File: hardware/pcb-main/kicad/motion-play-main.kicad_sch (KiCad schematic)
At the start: 26 parts, among them J2 DWEII Power Module, J3 LED_Strip, J4 Conn_01x05, J5 Conn_01x05, J6 Conn_01x05, U1 AP2112K-3.3TRG1, U2 T-Display-S3

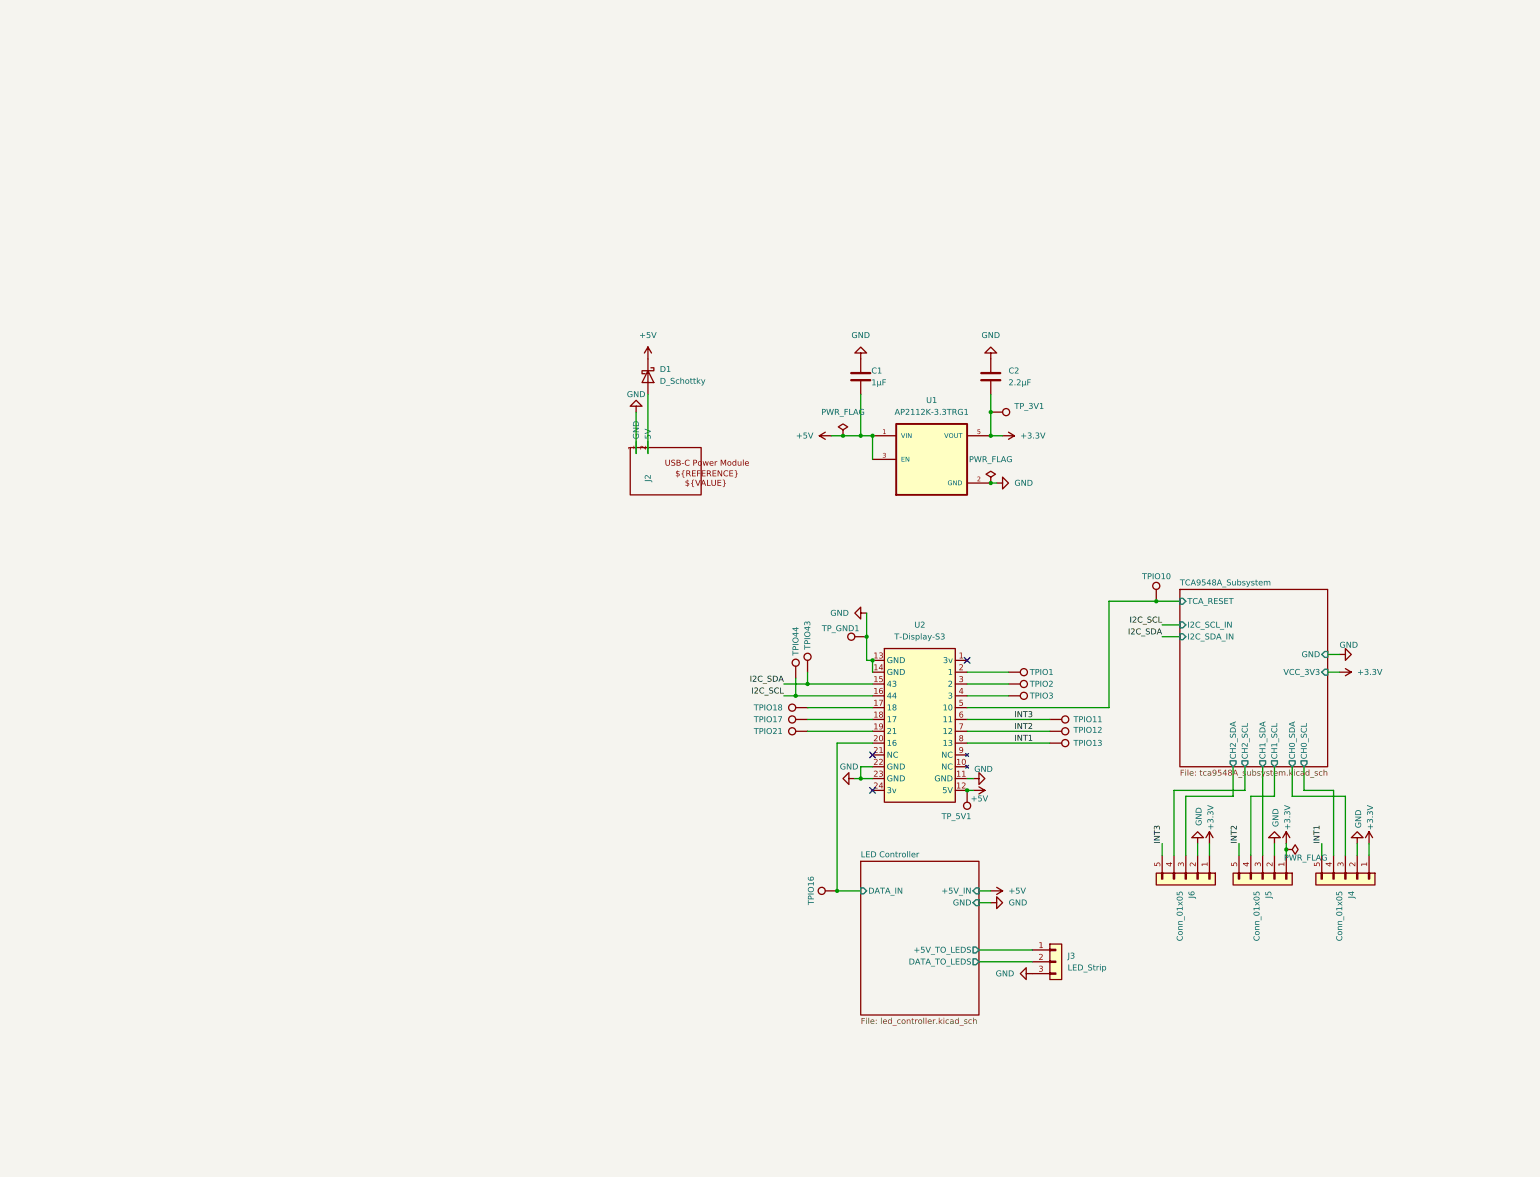
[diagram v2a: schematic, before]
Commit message: Complete Phase 3a: annotate power, MCU, I2C mux, and sensor connector blocks
Annotated 31/37 components across 4 functional blocks (power, mcu, i2c_mux,
sensor_connectors) with ai_function, ai_block, ai_role, and ai_critical_specs
properties. Remaining 6 components are LED controller block (Phase 3b).
Added 10 verification test questions for Phase 3c. KiCad round-trip confirmed
all ai_ properties survive native save.

Made-with: Cursor
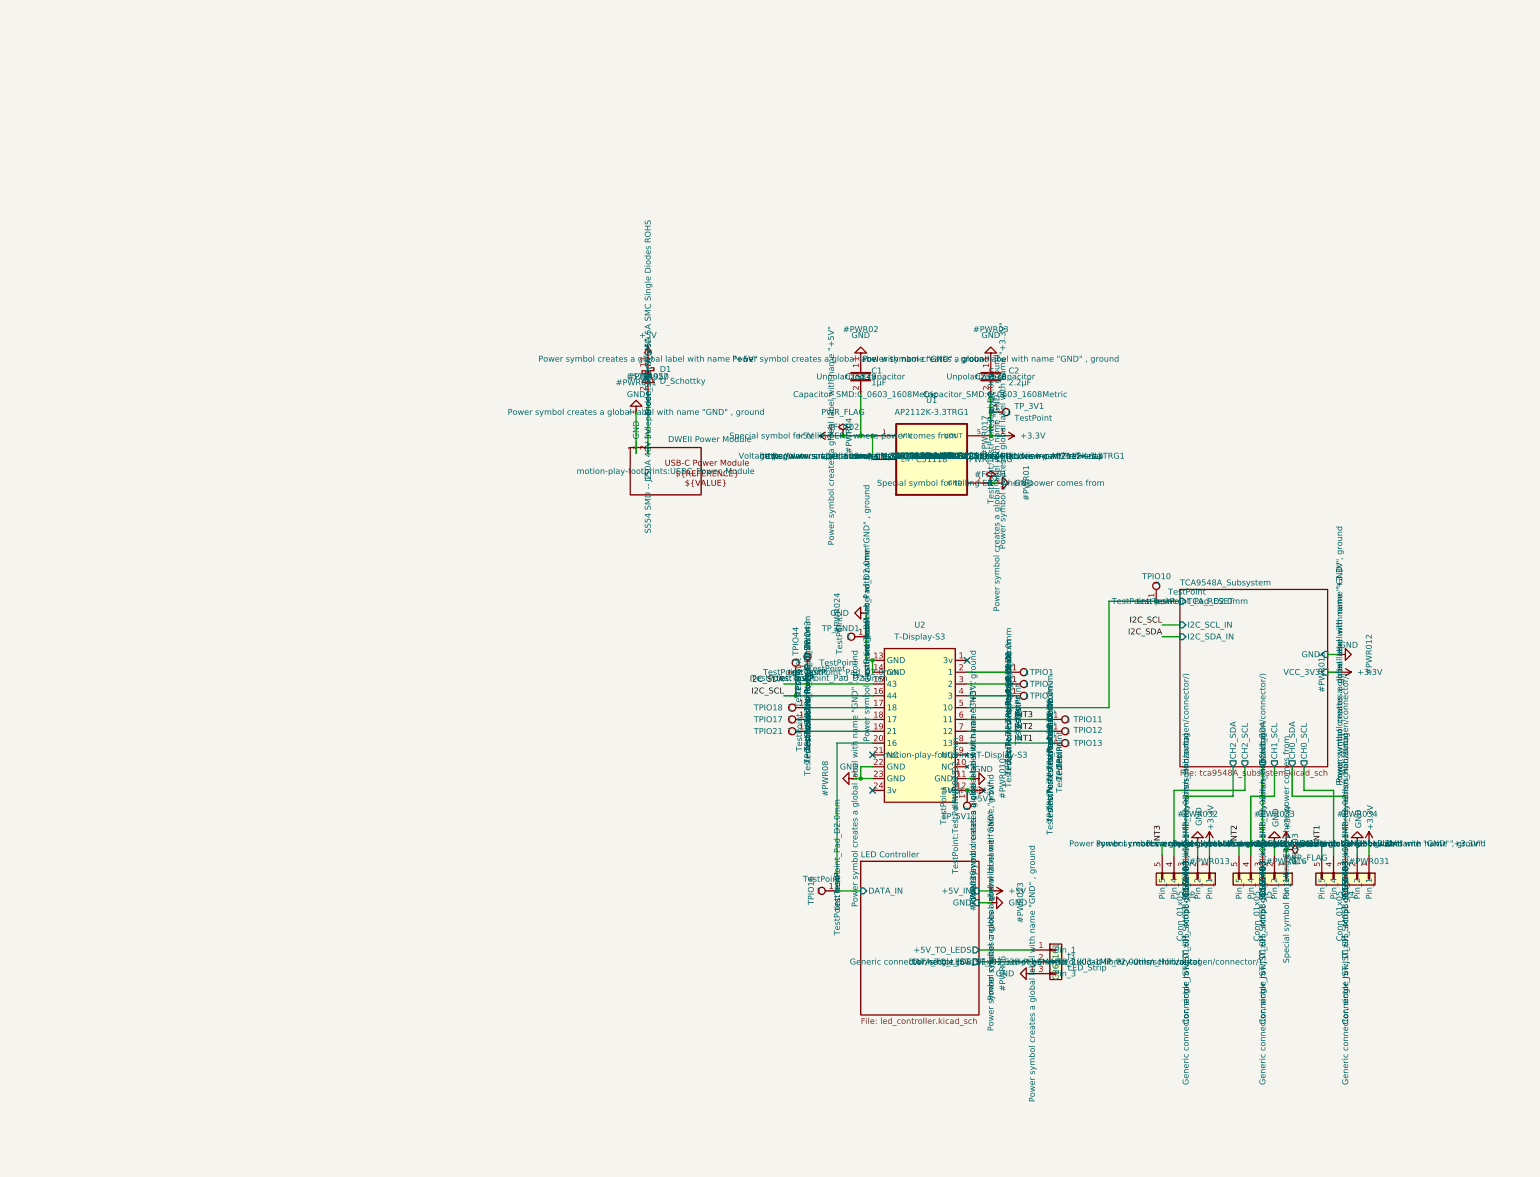
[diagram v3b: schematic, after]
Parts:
- C1: ai_block (none) -> power; ai_critical_specs (none) -> 1uF, 0603; ai_function (none) -> Input bypass capacitor for U1 voltage regulator; ai_role (none) -> decoupling
- C2: ai_block (none) -> power; ai_critical_specs (none) -> 2.2uF, 0603, required for LDO stability; ai_function (none) -> Output stabilization capacitor for U1 voltage regulator; ai_role (none) -> decoupling
- D1: ai_block (none) -> power; ai_critical_specs (none) -> Schottky, low Vf (~0.3V), handles full system current; ai_function (none) -> Reverse-polarity protection diode between power module and 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; ai_role (none) -> protection
- J2: ai_block (none) -> power; ai_critical_specs (none) -> 5V output, ~2.4A max, includes battery charging circuit; ai_function (none) -> USB-C power input module with battery charging, provides 5V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
- J4: ai_block (none) -> sensor_connectors; ai_critical_specs (none) -> 5-pin: 3.3V, GND, CH0_SDA, CH0_SCL, INT1; ai_function (none) -> JST-SH connector to sensor module 1 (M1, 6 oclock position)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; ai_role (none) -> connector
- J5: ai_block (none) -> sensor_connectors; ai_critical_specs (none) -> 5-pin: 3.3V, GND, CH1_SDA, CH1_SCL, INT2; ai_function (none) -> JST-SH connector to sensor module 2 (M2, 9 oclock position)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; ai_role (none) -> connector
- J6: ai_block (none) -> sensor_connectors; ai_critical_specs (none) -> 5-pin: 3.3V, GND, CH2_SDA, CH2_SCL, INT3; ai_function (none) -> JST-SH connector to sensor module 3 (M3, 3 oclock position)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; ai_role (none) -> connector
- TPIO1: ai_block (none) -> mcu; ai_function (none) -> GPIO 1 breakout test point (unused); ai_role (none) -> test_point
- TPIO10: ai_block (none) -> mcu; ai_function (none) -> TCA9548A reset signal test point; ai_role (none) -> test_point
- TPIO11: ai_block (none) -> mcu; ai_function (none) -> Sensor module 3 interrupt test point; ai_role (none) -> test_point
- TPIO12: ai_block (none) -> mcu; ai_function (none) -> Sensor module 2 interrupt test point; ai_role (none) -> test_point
- TPIO13: ai_block (none) -> mcu; ai_function (none) -> Sensor module 1 interrupt test point; ai_role (none) -> test_point
- TPIO16: ai_block (none) -> mcu; ai_function (none) -> LED data output (GPIO 16) test point; ai_role (none) -> test_point
- TPIO17: ai_block (none) -> mcu; ai_function (none) -> GPIO 17 breakout test point (unused); ai_role (none) -> test_point
- TPIO18: ai_block (none) -> mcu; ai_function (none) -> GPIO 18 breakout test point (unused); ai_role (none) -> test_point
- TPIO2: ai_block (none) -> mcu; ai_function (none) -> GPIO 2 breakout test point (unused); ai_role (none) -> test_point
- TPIO21: ai_block (none) -> mcu; ai_function (none) -> GPIO 21 breakout test point (unused); ai_role (none) -> test_point
- TPIO3: ai_block (none) -> mcu; ai_function (none) -> GPIO 3 breakout test point (unused); ai_role (none) -> test_point
- TPIO43: ai_block (none) -> mcu; ai_function (none) -> I2C SDA (GPIO 43) test point; ai_role (none) -> test_point
- TPIO44: ai_block (none) -> mcu; ai_function (none) -> I2C SCL (GPIO 44) test point; ai_role (none) -> test_point
- TP_3V1: ai_block (none) -> power; ai_function (none) -> Test point for +3.3V power rail; ai_role (none) -> test_point
- TP_5V1: ai_block (none) -> power; ai_function (none) -> Test point for +5V power rail; ai_role (none) -> test_point
- TP_GND1: ai_block (none) -> power; ai_function (none) -> Test point for ground rail; ai_role (none) -> test_point
- U1: ai_block (none) -> power; ai_critical_specs (none) -> 3.3V output, 600mA max, dropout ~250mV, input from +5V; ai_function (none) -> 3.3V LDO regulator for sensor and I2C bus power; ai_role (none) -> voltage_regulator
- U2: ai_block (none) -> mcu; ai_critical_specs (none) -> ESP32-S3, dual-core 240MHz, WiFi+BT, built-in 1.9in LCD, PS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; ai_function (none) -> Main system controller (LilyGO T-Display-S3 ESP32-S3 dev bo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; ai_role (none) -> controller

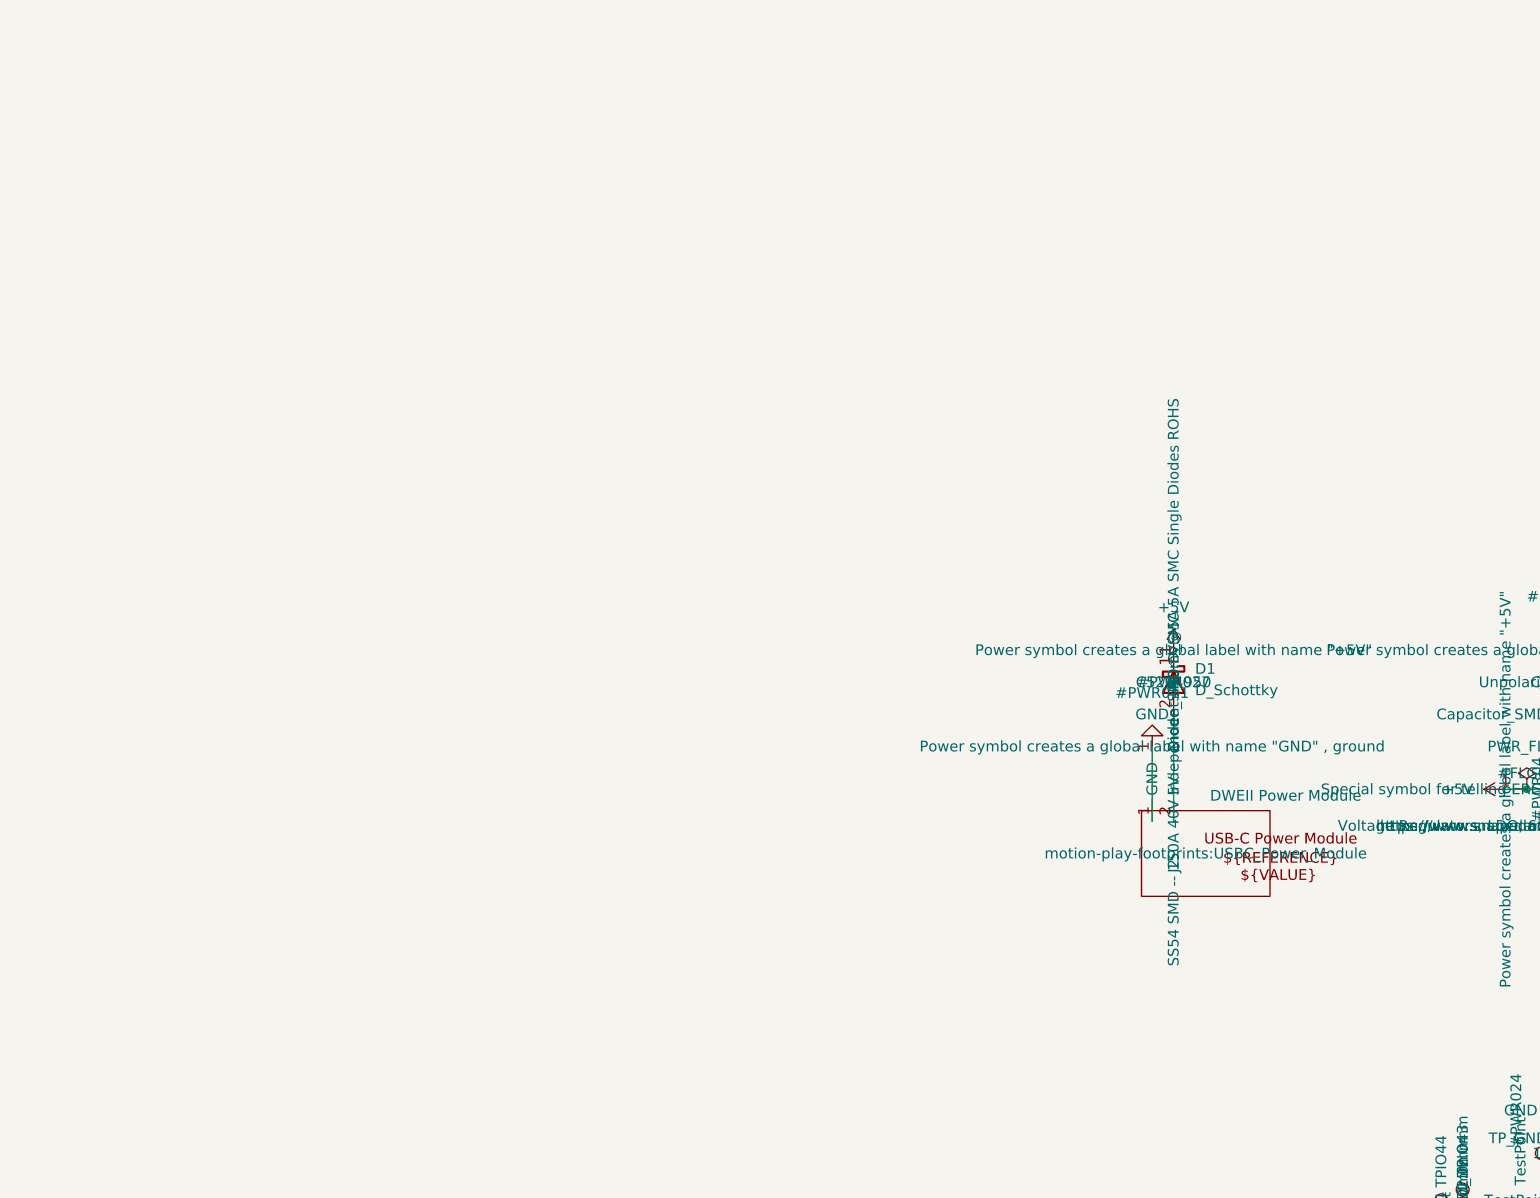
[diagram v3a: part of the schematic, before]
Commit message: Complete Phase 3b: annotate LED controller block, nets, and functional blocks
- Annotated final 6 components (IC1 level shifter, F1 fuse, R27 sense
  resistor, C7/C8 caps, J3 LED connector) → 37/37 components (100%)
- Added net annotations for all 26 nets (type, protocol, direction, description)
- Defined 5 functional blocks: power, mcu, i2c_mux, sensor_connectors,
  led_controller — with descriptions, component membership, and design notes
- Added top-level description and sheet_interface descriptions
- Re-extracted with --previous merge; KiCad round-trip save applied to all sheets

Made-with: Cursor
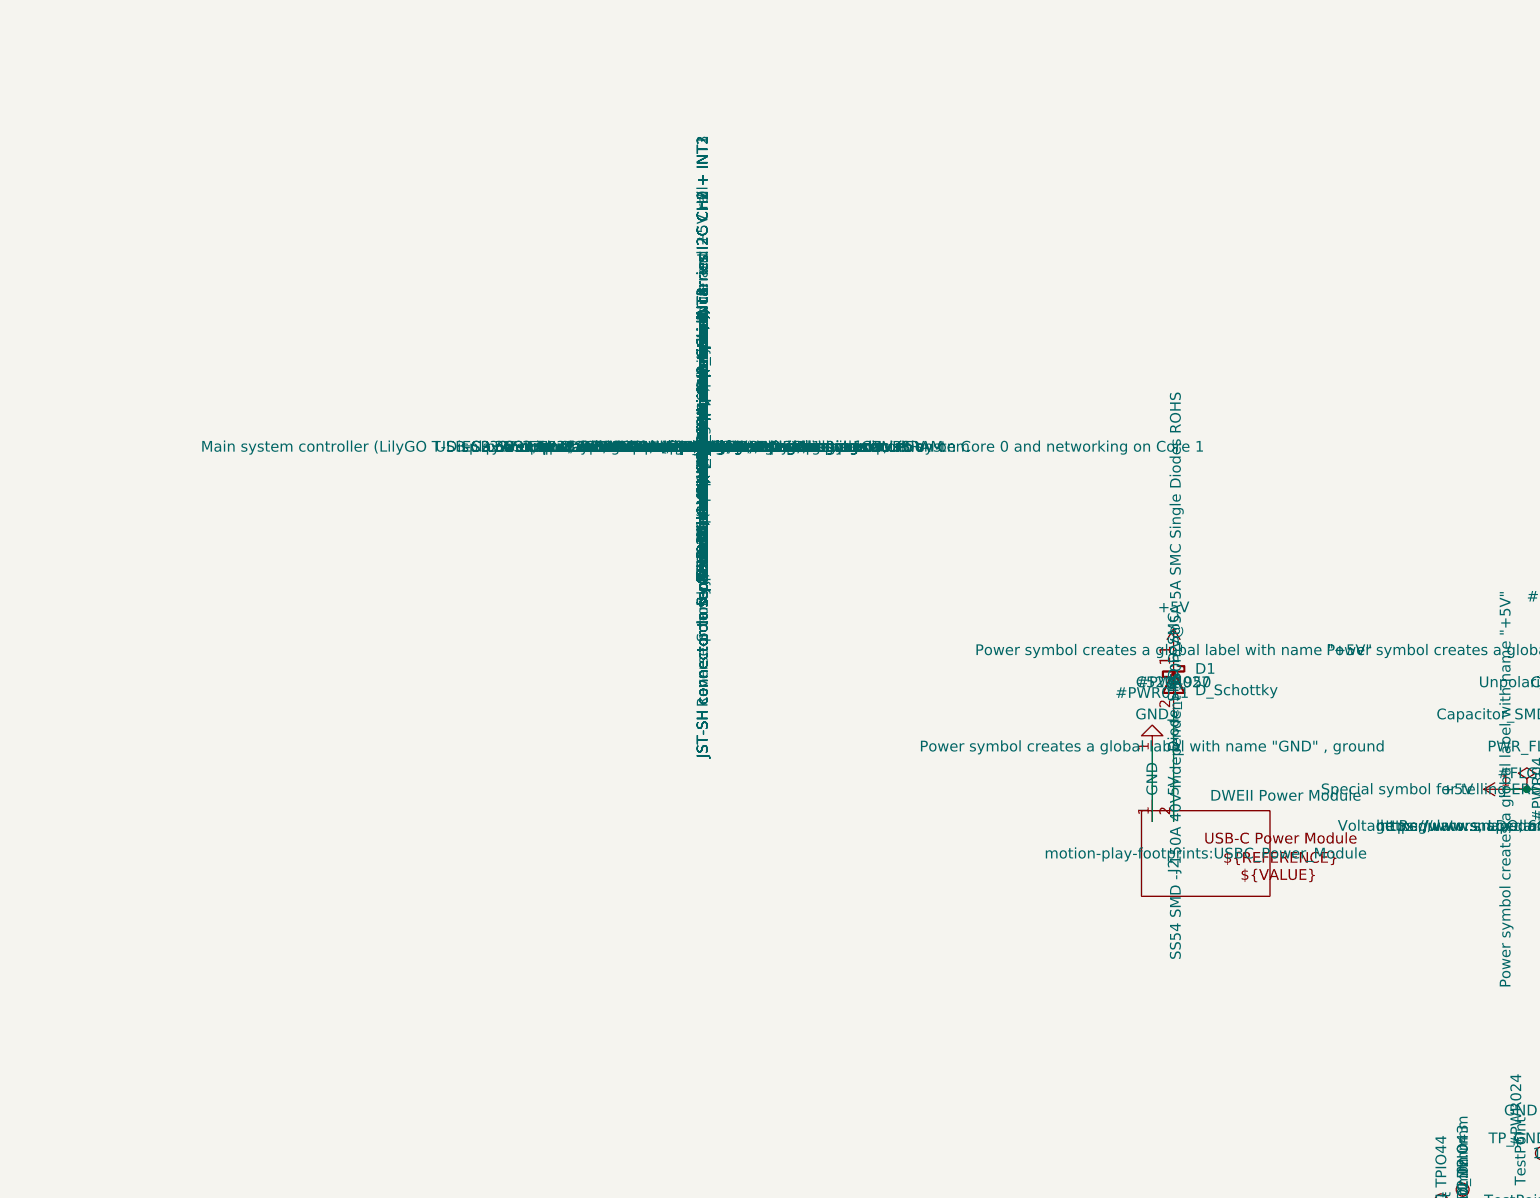
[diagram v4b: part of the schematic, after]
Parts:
- J3: ai_block (none) -> led_controller; ai_critical_specs (none) -> 3-pin: +5V_TO_LEDS, DATA_TO_LEDS, GND; ai_function (none) -> JST-PH connector to WS2812B LED strip (72 LEDs, 1.2m), carr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; ai_role (none) -> connector
